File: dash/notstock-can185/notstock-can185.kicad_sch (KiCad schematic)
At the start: 31 parts, among them J1 OBD 12V GND H L 15, J2 UART wires from display, J3 BAT to display, U1 LMR16006YDDCR, U2 SN65HVD230

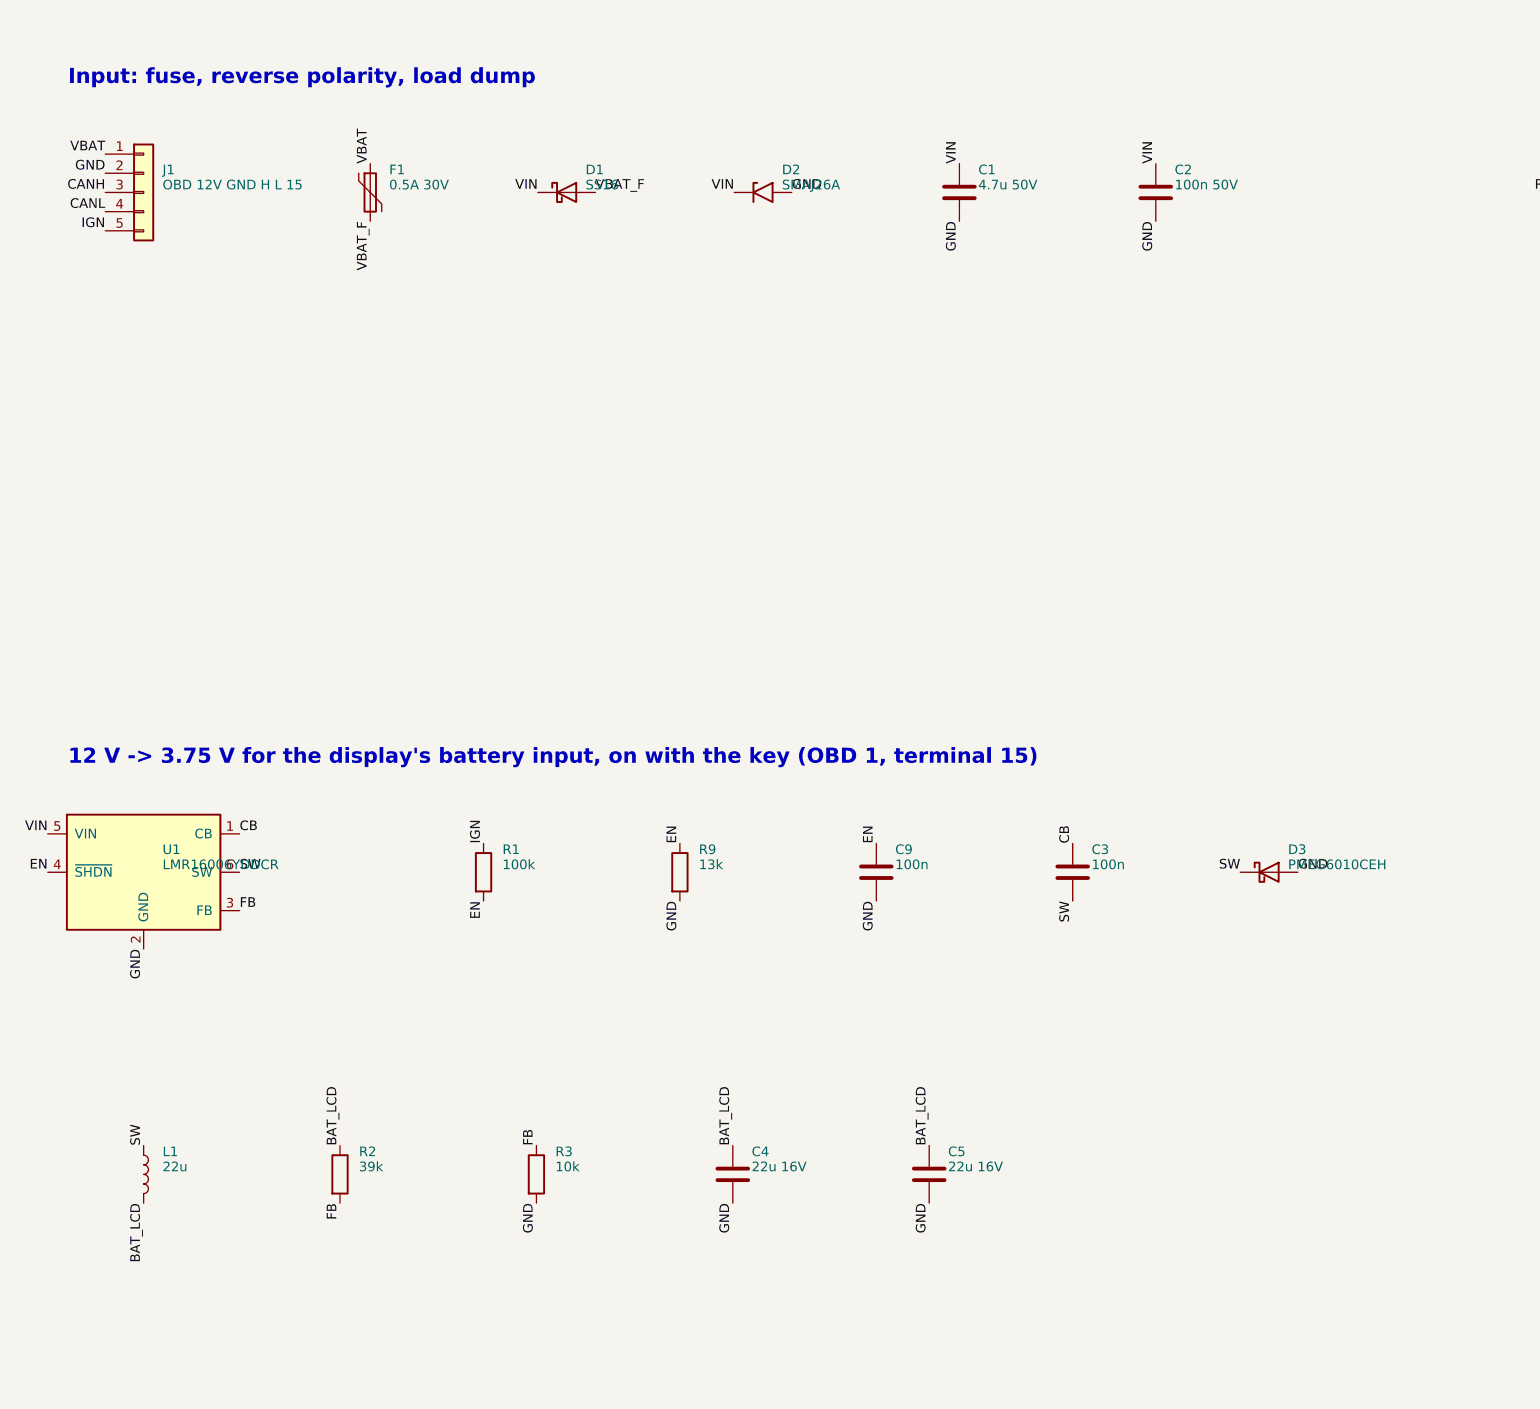
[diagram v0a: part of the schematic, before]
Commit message: CAN 1.85 rev 6: 12 V from OBD pin 1 (terminal 15), 4-pin J1 again
The board takes its supply from the key-switched pin 1 instead of the
permanent pin 16, so the ignition input and its divider are not needed.

Co-Authored-By: Claude Opus 5.5 <noreply@anthropic.com>
Claude-Session: https://claude.ai/code/session_018SKN4tJhAPpVCWtvRZgZpD
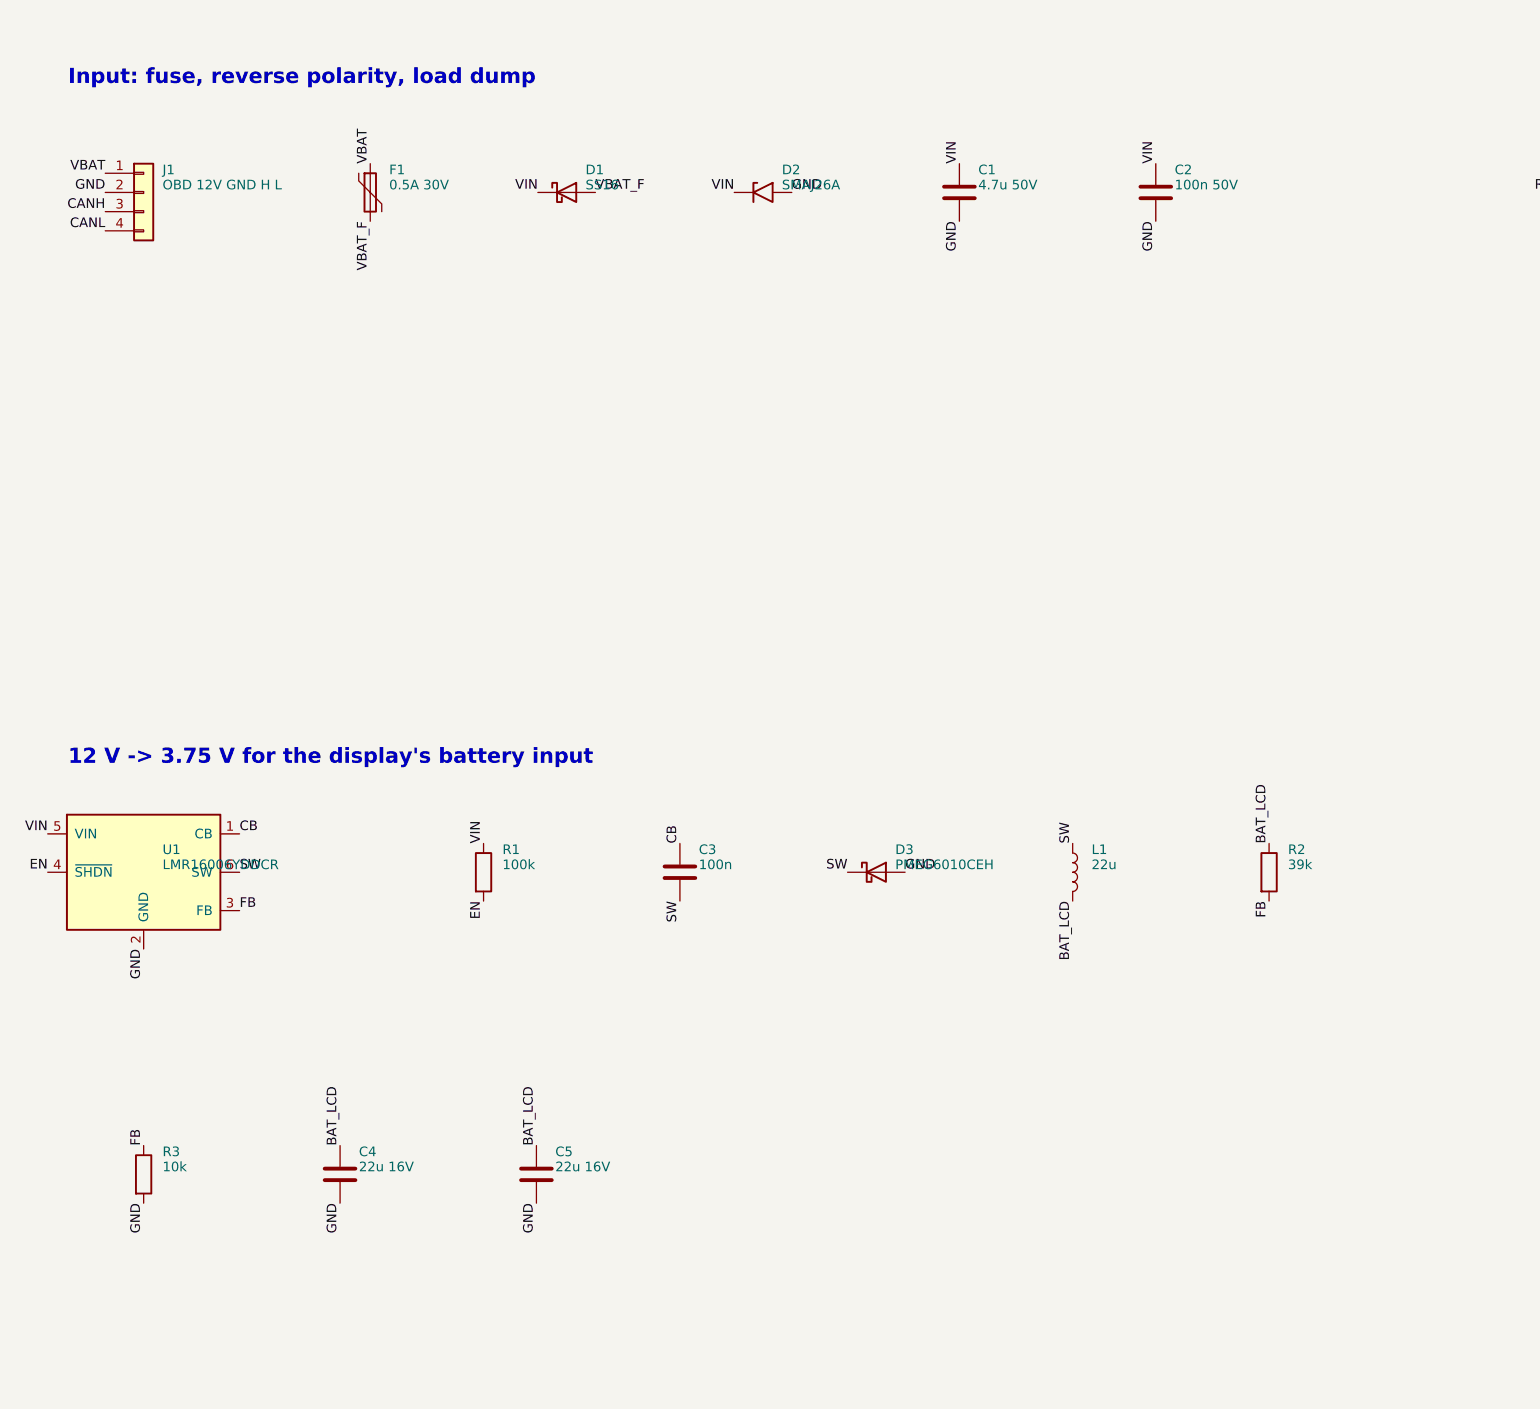
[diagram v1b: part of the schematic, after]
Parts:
- removed C9: 100n, Capacitor_SMD:C_0603_1608Metric, symbol Device:C
- removed R9: 13k, Resistor_SMD:R_0603_1608Metric, symbol Device:R
- J1: value OBD 12V GND H L 15 -> OBD 12V GND H L; footprint Connector_JST:JST_PH_B5B-PH-SM4-TB_1x05-1MP_P2.00mm_Vertical -> Connector_JST:JST_PH_B4B-PH-SM4-TB_1x04-1MP_P2.00mm_Vertical; symbol Connector_Generic:Conn_01x05 -> Connector_Generic:Conn_01x04; LCSC C265085 -> C160354; MPN JST B5B-PH-SM4-TB(LF)(SN) -> JST B4B-PH-SM4-TB(LF)(SN)
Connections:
- net VIN: now also R1.1
- removed net IGN: J1.5 (Pin_5), R1.1
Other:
- note added: "12 V -> 3.75 V for the display's battery input"
- note removed: "12 V -> 3.75 V for the display's battery input, on with the key (OBD 1, terminal 15)"
- moved on the sheet: C3, C4, C5, D3, L1, R2, R3

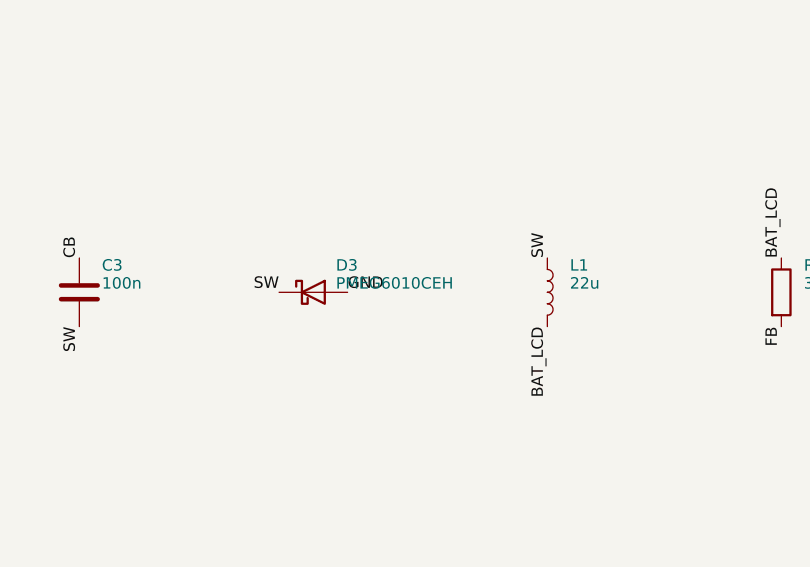
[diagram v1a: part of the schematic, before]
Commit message: CAN boards: D3 K16 (C2943756) for the PMEG6010CEH out of stock
Same footprint (SOD-123FL on the SOD-123F pads), 60 V 1 A Schottky.
BOM, schematic and the boards' LCSC fields updated on both boards.

Co-Authored-By: Claude Opus 5.5 <noreply@anthropic.com>
Claude-Session: https://claude.ai/code/session_018SKN4tJhAPpVCWtvRZgZpD
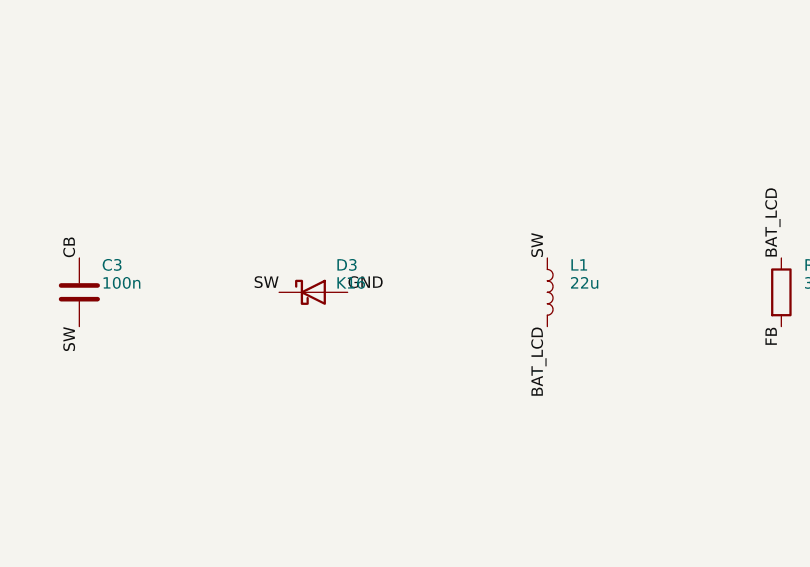
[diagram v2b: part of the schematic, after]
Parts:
- D3: value PMEG6010CEH -> K16; LCSC C110797 -> C2943756; MPN Nexperia PMEG6010CEH,115 -> GOODWORK K16 (60 V 1 A Schottky, SOD-123FL)
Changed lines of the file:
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@@
     (property "Reference" "D3" (at 129.5 137 0)
       (effects (font (size 1.27 1.27)) (justify left)))
-    (property "Value" "PMEG6010CEH" (at 129.5 139 0)
+    (property "Value" "K16" (at 129.5 139 0)
       (effects (font (size 1.27 1.27)) (justify left)))
     (property "Footprint" "Diode_SMD:D_SOD-123F" (at 127 140 0)
@@
     (property "Datasheet" "~" (at 127 140 0)
       (effects (font (size 1.27 1.27)) hide))
-    (property "LCSC" "C110797" (at 127 140 0)
+    (property "LCSC" "C2943756" (at 127 140 0)
       (effects (font (size 1.27 1.27)) hide))
-    (property "MPN" "Nexperia PMEG6010CEH,115" (at 127 140 0)
+    (property "MPN" "GOODWORK K16 (60 V 1 A Schottky, SOD-123FL)" (at 127 140 0)
       (effects (font (size 1.27 1.27)) hide))
     (pin "1")

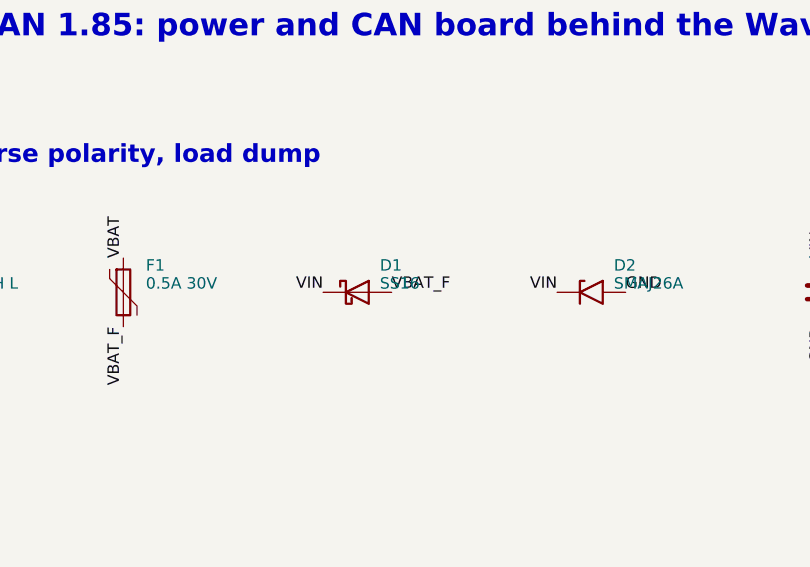
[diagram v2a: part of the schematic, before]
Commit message: CAN boards: JLCPCB basic parts where possible
D1 SS16 -> SS34 (C8678, basic, same SMA footprint) on both boards.
CAN 1.32: C4/C5 22 uF 1206 -> 0805 25 V (C45783, basic), rerouted,
DRC clean.

Co-Authored-By: Claude Opus 5.5 <noreply@anthropic.com>
Claude-Session: https://claude.ai/code/session_018SKN4tJhAPpVCWtvRZgZpD
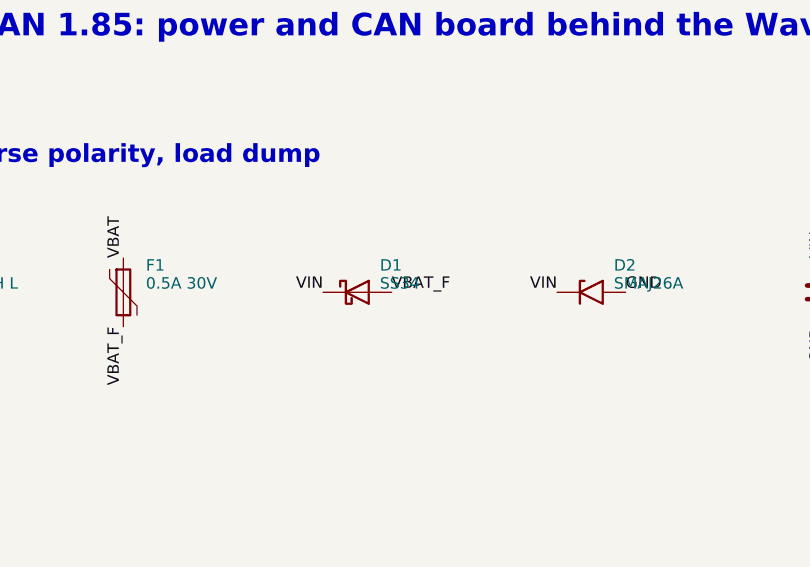
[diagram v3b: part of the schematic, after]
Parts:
- D1: value SS16 -> SS34; LCSC C2758574 -> C8678; MPN UMW SS16 (60 V 1 A) -> MDD SS34 (40 V 3 A)
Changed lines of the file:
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@@
     (property "Reference" "D1" (at 88.5 47 0)
       (effects (font (size 1.27 1.27)) (justify left)))
-    (property "Value" "SS16" (at 88.5 49 0)
+    (property "Value" "SS34" (at 88.5 49 0)
       (effects (font (size 1.27 1.27)) (justify left)))
     (property "Footprint" "Diode_SMD:D_SMA" (at 86 50 0)
@@
     (property "Datasheet" "~" (at 86 50 0)
       (effects (font (size 1.27 1.27)) hide))
-    (property "LCSC" "C2758574" (at 86 50 0)
+    (property "LCSC" "C8678" (at 86 50 0)
       (effects (font (size 1.27 1.27)) hide))
-    (property "MPN" "UMW SS16 (60 V 1 A)" (at 86 50 0)
+    (property "MPN" "MDD SS34 (40 V 3 A)" (at 86 50 0)
       (effects (font (size 1.27 1.27)) hide))
     (pin "1")
